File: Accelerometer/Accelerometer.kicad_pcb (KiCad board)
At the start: 2 copper layers, 50 x 31 mm, 8 parts, among them U1 KX134-1211

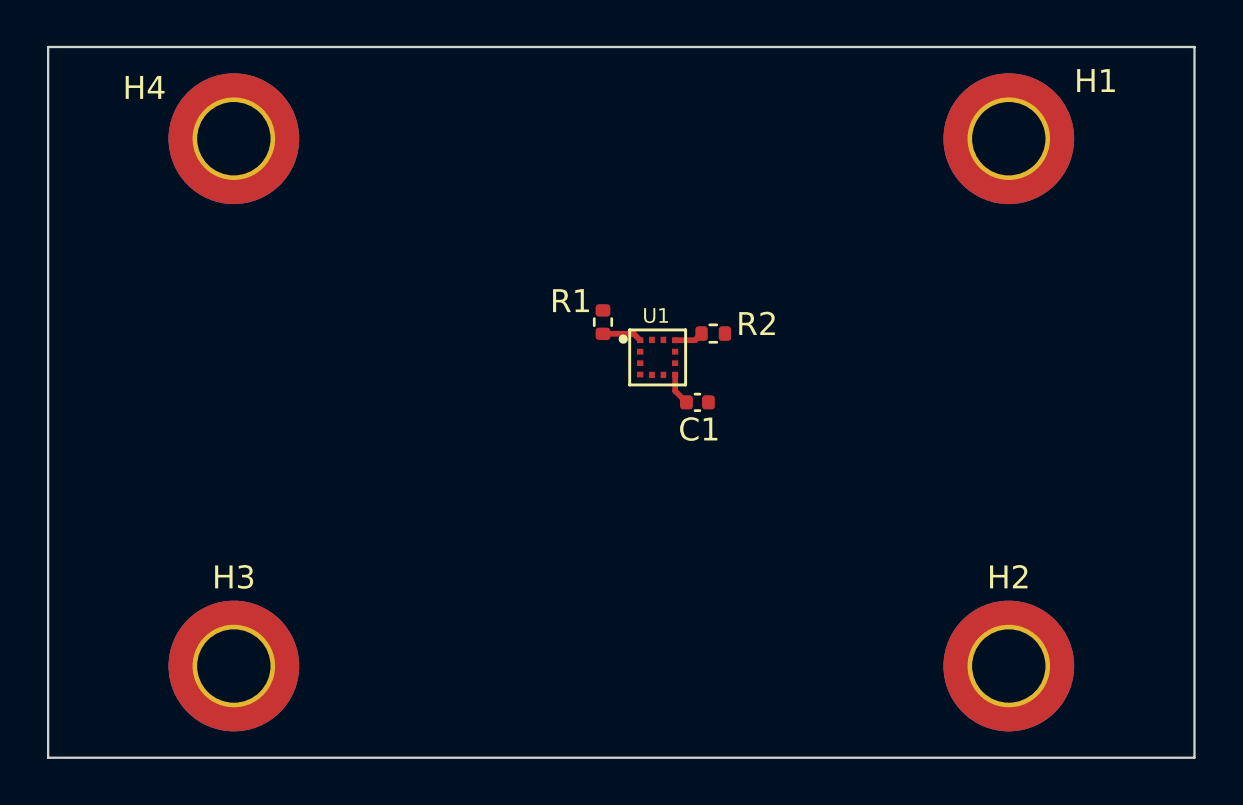
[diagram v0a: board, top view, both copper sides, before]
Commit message: Route sensors, IMU and radio board
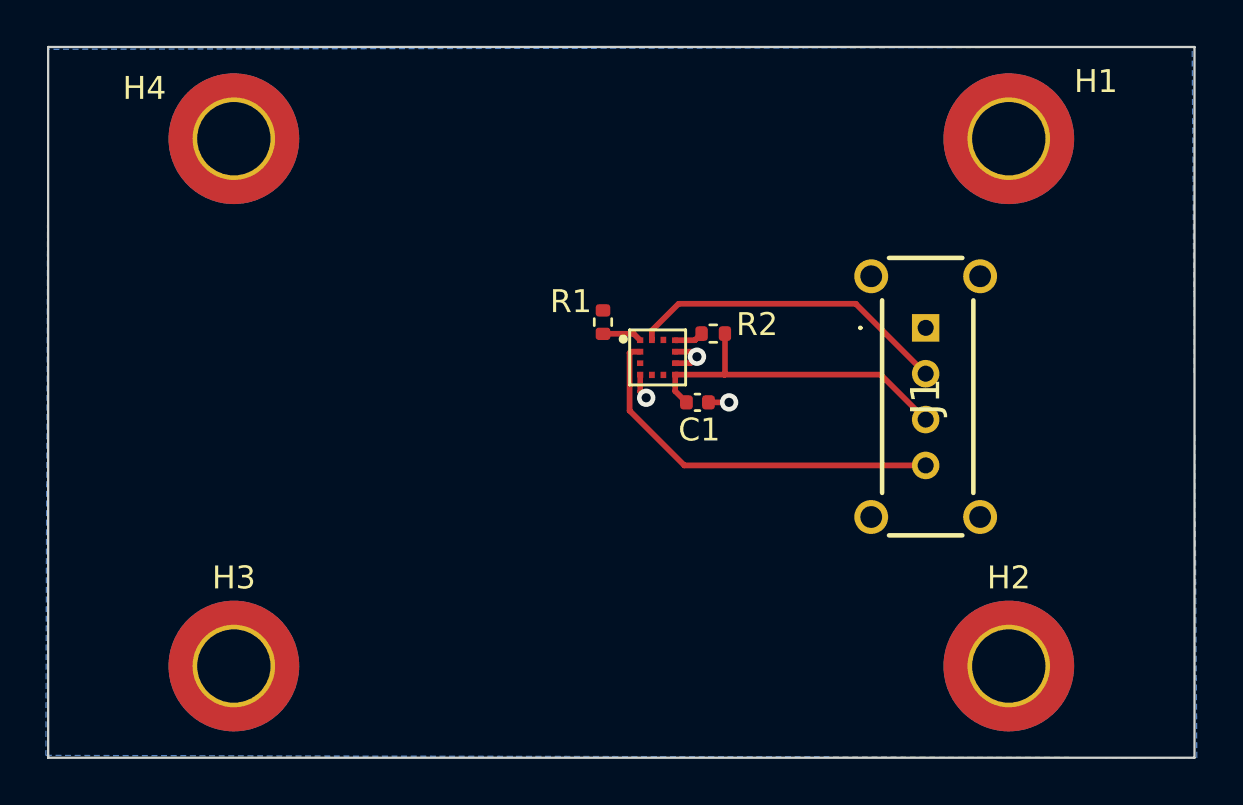
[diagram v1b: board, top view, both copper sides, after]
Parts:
- added J1: M80-8770405, KiCad:M808770405, F.Cu at (151.1, 88.7)
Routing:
- net /SDA: track 0.00 -> 16.9 mm
- net /SCL: track 0.00 -> 14.1 mm
- net +3.3V: track 1.41 -> 15.0 mm
- net GND: track 0.00 -> 4.13 mm, vias 0 -> 3
- added copper zone on B.Cu, net GND
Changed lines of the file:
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@@
   (net 8 "unconnected-(U1-NC-Pad11)")
   (net 9 "/SCL")
+  (net 10 "unconnected-(J1-Pad1)")
+  (net 11 "unconnected-(J1-PadMH1)")
+  (net 12 "unconnected-(J1-PadMH2)")
+  (net 13 "unconnected-(J1-PadMH3)")
+  (net 14 "unconnected-(J1-PadMH4)")
   (footprint "Resistor_SMD:R_0402_1005Metric" (layer "F.Cu")
     (at 141.81 88.9)
@@
       (pinfunction "1") (pintype "input"))
   )
+  (footprint "KiCad:M808770405" (layer "F.Cu")
+    (at 151.075 88.65 90)
+    (descr "M80-8770405-2")
+    (tags "Connector")
+    (property "Arrow Part Number" "")
+    (property "Arrow Price/Stock" "")
+    (property "Height" "5.56")
+    (property "Manufacturer_Name" "Harwin")
+    (property "Manufacturer_Part_Number" "M80-8770405")
+    (property "Mouser Part Number" "855-M80-8770405")
+    (property "Mouser Price/Stock" "https://www.mouser.co.uk/ProductDetail/Harwin/M80-8770405?qs=3tymCvhQ29ZPq83M%252Bf8kIA%3D%3D")
+    (property "Sheetfile" "Accelerometer.kicad_sch")
+    (property "Sheetname" "")
+    (property "ki_description" "Datamate L-Tek SIL Male Vertical 3mm Throughboard Connector, latched, gold, 4 contacts")
+    (attr through_hole)
+    (fp_text reference "J1" (at -3 0 90) (layer "F.SilkS")
+        (effects (font (size 1.27 1.27) (thickness 0.254)))
+    )
+    (fp_text value "M80-8770405" (at -3 0 90) (layer "F.SilkS") hide
+        (effects (font (size 1.27 1.27) (thickness 0.254)))
+    )
+    (fp_text user "${REFERENCE}" (at -3 0 90) (layer "F.Fab")
+        (effects (font (size 1.27 1.27) (thickness 0.254)))
+    )
+    (fp_line (start -9.05 1.6) (end -9.05 -1.6)
+      (stroke (width 0.2) (type solid)) (layer "F.SilkS"))
+    (fp_line (start 0 -2.9) (end 0 -2.9)
+      (stroke (width 0.1) (type solid)) (layer "F.SilkS"))
+    (fp_line (start 0 -2.8) (end 0 -2.8)
+      (stroke (width 0.1) (type solid)) (layer "F.SilkS"))
+    (fp_line (start 1.2 -1.9) (end -7.2 -1.9)
+      (stroke (width 0.2) (type solid)) (layer "F.SilkS"))
+    (fp_line (start 1.2 2.08) (end -7.2 2.08)
+      (stroke (width 0.2) (type solid)) (layer "F.SilkS"))
+    (fp_line (start 3.05 -1.6) (end 3.05 1.6)
+      (stroke (width 0.2) (type solid)) (layer "F.SilkS"))
+    (fp_arc (start 0 -2.9) (mid 0.05 -2.85) (end 0 -2.8)
+      (stroke (width 0.1) (type solid)) (layer "F.SilkS"))
+    (fp_arc (start 0 -2.8) (mid -0.05 -2.85) (end 0 -2.9)
+      (stroke (width 0.1) (type solid)) (layer "F.SilkS"))
+    (fp_line (start -10.05 -4.114) (end -10.05 4.114)
+      (stroke (width 0.1) (type solid)) (layer "F.CrtYd"))
+    (fp_line (start -10.05 4.114) (end 4.05 4.114)
+      (stroke (width 0.1) (type solid)) (layer "F.CrtYd"))
+    (fp_line (start 4.05 -4.114) (end -10.05 -4.114)
+      (stroke (width 0.1) (type solid)) (layer "F.CrtYd"))
+    (fp_line (start 4.05 4.114) (end 4.05 -4.114)
+      (stroke (width 0.1) (type solid)) (layer "F.CrtYd"))
+    (fp_line (start -9.05 -1.9) (end 3.05 -1.9)
+      (stroke (width 0.1) (type solid)) (layer "F.Fab"))
+    (fp_line (start -9.05 2.08) (end -9.05 -1.9)
+      (stroke (width 0.1) (type solid)) (layer "F.Fab"))
+    (fp_line (start 3.05 -1.9) (end 3.05 2.08)
+      (stroke (width 0.1) (type solid)) (layer "F.Fab"))
+    (fp_line (start 3.05 2.08) (end -9.05 2.08)
+      (stroke (width 0.1) (type solid)) (layer "F.Fab"))
+    (pad "1" thru_hole rect (at 0 0 90) (size 1.2 1.2) (drill 0.7) (layers "*.Cu" "*.Mask")
+      (net 10 "unconnected-(J1-Pad1)") (pinfunction "1") (pintype "passive+no_connect"))
+    (pad "2" thru_hole circle (at -2 0 90) (size 1.2 1.2) (drill 0.7) (layers "*.Cu" "*.Mask")
+      (net 9 "/SCL") (pinfunction "2") (pintype "passive"))
+    (pad "3" thru_hole circle (at -4 0 90) (size 1.2 1.2) (drill 0.7) (layers "*.Cu" "*.Mask")
+      (net 1 "+3.3V") (pinfunction "3") (pintype "passive"))
+    (pad "4" thru_hole circle (at -6 0 90) (size 1.2 1.2) (drill 0.7) (layers "*.Cu" "*.Mask")
+      (net 5 "/SDA") (pinfunction "4") (pintype "passive"))
+    (pad "MH1" thru_hole circle (at 2.25 -2.375 90) (size 1.478 1.478) (drill 0.95) (layers "*.Cu" "*.Mask")
+      (net 11 "unconnected-(J1-PadMH1)") (pinfunction "MH1") (pintype "passive+no_connect"))
+    (pad "MH2" thru_hole circle (at 2.25 2.375 90) (size 1.478 1.478) (drill 0.95) (layers "*.Cu" "*.Mask")
+      (net 12 "unconnected-(J1-PadMH2)") (pinfunction "MH2") (pintype "passive+no_connect"))
+    (pad "MH3" thru_hole circle (at -8.25 2.375 90) (size 1.478 1.478) (drill 0.95) (layers "*.Cu" "*.Mask")
+      (net 13 "unconnected-(J1-PadMH3)") (pinfunction "MH3") (pintype "passive+no_connect"))
+    (pad "MH4" thru_hole circle (at -8.25 -2.375 90) (size 1.478 1.478) (drill 0.95) (layers "*.Cu" "*.Mask")
+      (net 14 "unconnected-(J1-PadMH4)") (pinfunction "MH4") (pintype "passive+no_connect"))
+    (model "M80-8770405.stp"
+      (offset (xyz 0 0 0))
+      (scale (xyz 1 1 1))
+      (rotate (xyz 0 0 0))
+    )
+  )
   (footprint "XDCR_KX003-1077:XDCR_KX003-1077" (layer "F.Cu")
     (at 139.385 89.94)
@@
     (property "ki_keywords" "KX134-1211")
     (attr smd)
-    (fp_text reference "U1" (at -0.068 -1.8064) (layer "F.SilkS")
+    (fp_text reference "U1" (at -0.068 -1.8064) (layer "F.SilkS") hide
         (effects (font (size 0.64 0.64) (thickness 0.15)))
     )
@@
     (stroke (width 0.1) (type default)) (layer "Edge.Cuts"))
   (segment (start 140.1475 90.69) (end 140.1475 91.4075) (width 0.25) (layer "F.Cu") (net 1))
+  (segment (start 142.32 90.67) (end 142.3 90.69) (width 0.25) (layer "F.Cu") (net 1))
+  (segment (start 149.115 90.69) (end 151.075 92.65) (width 0.25) (layer "F.Cu") (net 1))
+  (segment (start 142.32 88.9) (end 142.32 90.67) (width 0.25) (layer "F.Cu") (net 1))
+  (segment (start 140.1475 90.69) (end 142.3 90.69) (width 0.25) (layer "F.Cu") (net 1))
+  (segment (start 142.3 90.69) (end 149.115 90.69) (width 0.25) (layer "F.Cu") (net 1))
   (segment (start 140.1475 91.4075) (end 140.64 91.9) (width 0.25) (layer "F.Cu") (net 1))
+  (segment (start 140.1475 90.19) (end 140.818393 90.19) (width 0.25) (layer "F.Cu") (net 2))
+  (segment (start 140.818393 90.19) (end 141.099434 89.908959) (width 0.25) (layer "F.Cu") (net 2))
+  (segment (start 138.6225 90.69) (end 138.6225 91.438) (width 0.25) (layer "F.Cu") (net 2))
+  (segment (start 138.6225 91.438) (end 138.8845 91.7) (width 0.25) (layer "F.Cu") (net 2))
+  (segment (start 140.880475 89.69) (end 141.099434 89.908959) (width 0.25) (layer "F.Cu") (net 2))
+  (segment (start 141.6 91.9) (end 142.5 91.9) (width 0.25) (layer "F.Cu") (net 2))
+  (segment (start 140.1475 89.69) (end 140.880475 89.69) (width 0.25) (layer "F.Cu") (net 2))
+  (via (at 138.8845 91.7) (size 0.8) (drill 0.4) (layers "F.Cu" "B.Cu") (net 2))
+  (via (at 141.099434 89.908959) (size 0.8) (drill 0.4) (layers "F.Cu" "B.Cu") (net 2))
+  (via (at 142.5 91.9) (size 0.8) (drill 0.4) (layers "F.Cu" "B.Cu") (net 2))
   (segment (start 137 88.91) (end 138.3425 88.91) (width 0.25) (layer "F.Cu") (net 3))
   (segment (start 138.3425 88.91) (end 138.6225 89.19) (width 0.25) (layer "F.Cu") (net 3))
   (segment (start 140.1475 89.19) (end 141.01 89.19) (width 0.25) (layer "F.Cu") (net 4))
   (segment (start 141.01 89.19) (end 141.3 88.9) (width 0.25) (layer "F.Cu") (net 4))
+  (segment (start 138.16 89.74) (end 138.16 92.26) (width 0.25) (layer "F.Cu") (net 5))
+  (segment (start 138.21 89.69) (end 138.16 89.74) (width 0.25) (layer "F.Cu") (net 5))
+  (segment (start 140.55 94.65) (end 151.075 94.65) (width 0.25) (layer "F.Cu") (net 5))
+  (segment (start 138.16 92.26) (end 140.55 94.65) (width 0.25) (layer "F.Cu") (net 5))
+  (segment (start 138.6225 89.69) (end 138.21 89.69) (width 0.25) (layer "F.Cu") (net 5))
+  (segment (start 139.135 89.1775) (end 139.135 88.765) (width 0.25) (layer "F.Cu") (net 9))
+  (segment (start 139.135 88.765) (end 140.3 87.6) (width 0.25) (layer "F.Cu") (net 9))
+  (segment (start 148.025 87.6) (end 151.075 90.65) (width 0.25) (layer "F.Cu") (net 9))
+  (segment (start 140.3 87.6) (end 148.025 87.6) (width 0.25) (layer "F.Cu") (net 9))
+  (zone (net 2) (net_name "GND") (layer "B.Cu") (hatch edge 0.5)
+    (connect_pads (clearance 0.3))
+    (min_thickness 0.25) (filled_areas_thickness no)
+    (fill yes (thermal_gap 0.5) (thermal_bridge_width 0.5))
+    (polygon
+      (pts
+        (xy 112.8 76.5)
+        (xy 112.7 107.3)
+        (xy 162.9 107.4)
+        (xy 162.7 76.4)
+      )
+    )
+  )
 )

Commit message: Done with most of the boards
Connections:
- J1 pad 1: unconnected-(J1-Pad1) -> GND
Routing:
- net GND: track 4.13 -> 30.6 mm
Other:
- board text added: "SCL"
- board text added: "SDA"
- board text added: "Vin"
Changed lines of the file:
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@@
   (net 8 "unconnected-(U1-NC-Pad11)")
   (net 9 "/SCL")
-  (net 10 "unconnected-(J1-Pad1)")
-  (net 11 "unconnected-(J1-PadMH1)")
-  (net 12 "unconnected-(J1-PadMH2)")
-  (net 13 "unconnected-(J1-PadMH3)")
-  (net 14 "unconnected-(J1-PadMH4)")
+  (net 10 "unconnected-(J1-PadMH1)")
+  (net 11 "unconnected-(J1-PadMH2)")
+  (net 12 "unconnected-(J1-PadMH3)")
+  (net 13 "unconnected-(J1-PadMH4)")
   (footprint "Resistor_SMD:R_0402_1005Metric" (layer "F.Cu")
     (at 141.81 88.9)
@@
       (stroke (width 0.1) (type solid)) (layer "F.Fab"))
     (pad "1" thru_hole rect (at 0 0 90) (size 1.2 1.2) (drill 0.7) (layers "*.Cu" "*.Mask")
-      (net 10 "unconnected-(J1-Pad1)") (pinfunction "1") (pintype "passive+no_connect"))
+      (net 2 "GND") (pinfunction "1") (pintype "passive"))
     (pad "2" thru_hole circle (at -2 0 90) (size 1.2 1.2) (drill 0.7) (layers "*.Cu" "*.Mask")
       (net 9 "/SCL") (pinfunction "2") (pintype "passive"))
@@
       (net 5 "/SDA") (pinfunction "4") (pintype "passive"))
     (pad "MH1" thru_hole circle (at 2.25 -2.375 90) (size 1.478 1.478) (drill 0.95) (layers "*.Cu" "*.Mask")
-      (net 11 "unconnected-(J1-PadMH1)") (pinfunction "MH1") (pintype "passive+no_connect"))
+      (net 10 "unconnected-(J1-PadMH1)") (pinfunction "MH1") (pintype "passive+no_connect"))
     (pad "MH2" thru_hole circle (at 2.25 2.375 90) (size 1.478 1.478) (drill 0.95) (layers "*.Cu" "*.Mask")
-      (net 12 "unconnected-(J1-PadMH2)") (pinfunction "MH2") (pintype "passive+no_connect"))
+      (net 11 "unconnected-(J1-PadMH2)") (pinfunction "MH2") (pintype "passive+no_connect"))
     (pad "MH3" thru_hole circle (at -8.25 2.375 90) (size 1.478 1.478) (drill 0.95) (layers "*.Cu" "*.Mask")
-      (net 13 "unconnected-(J1-PadMH3)") (pinfunction "MH3") (pintype "passive+no_connect"))
+      (net 12 "unconnected-(J1-PadMH3)") (pinfunction "MH3") (pintype "passive+no_connect"))
     (pad "MH4" thru_hole circle (at -8.25 -2.375 90) (size 1.478 1.478) (drill 0.95) (layers "*.Cu" "*.Mask")
-      (net 14 "unconnected-(J1-PadMH4)") (pinfunction "MH4") (pintype "passive+no_connect"))
+      (net 13 "unconnected-(J1-PadMH4)") (pinfunction "MH4") (pintype "passive+no_connect"))
     (model "M80-8770405.stp"
       (offset (xyz 0 0 0))
@@
   (gr_line (start 162.8 107.4) (end 162.8 76.4)
     (stroke (width 0.1) (type default)) (layer "Edge.Cuts"))
+  (gr_text "SDA" (at 144.6 95.5) (layer "F.SilkS")
+    (effects (font (size 1 1) (thickness 0.15)))
+  )
+  (gr_text "SCL" (at 145.6 86.9) (layer "F.SilkS")
+    (effects (font (size 0.9 0.8) (thickness 0.15)))
+  )
+  (gr_text "Vin" (at 145.2 89.9) (layer "F.SilkS")
+    (effects (font (size 1 1) (thickness 0.15)))
+  )
   (segment (start 140.1475 90.69) (end 140.1475 91.4075) (width 0.25) (layer "F.Cu") (net 1))
   (segment (start 142.32 90.67) (end 142.3 90.69) (width 0.25) (layer "F.Cu") (net 1))
@@
   (via (at 141.099434 89.908959) (size 0.8) (drill 0.4) (layers "F.Cu" "B.Cu") (net 2))
   (via (at 142.5 91.9) (size 0.8) (drill 0.4) (layers "F.Cu" "B.Cu") (net 2))
+  (segment (start 146.3 88.75) (end 146.4 88.65) (width 0.25) (layer "B.Cu") (net 2))
+  (segment (start 138.9 91.7) (end 141.3 94.1) (width 0.25) (layer "B.Cu") (net 2))
+  (segment (start 144.95 88.65) (end 146.4 88.65) (width 0.25) (layer "B.Cu") (net 2))
+  (segment (start 146.3 91.6) (end 146.3 88.75) (width 0.25) (layer "B.Cu") (net 2))
+  (segment (start 144.5 91.9) (end 146 91.9) (width 0.25) (layer "B.Cu") (net 2))
+  (segment (start 141.3 94.1) (end 144.4 94.1) (width 0.25) (layer "B.Cu") (net 2))
+  (segment (start 141.099434 89.908959) (end 143.691041 89.908959) (width 0.25) (layer "B.Cu") (net 2))
+  (segment (start 143.691041 89.908959) (end 144.95 88.65) (width 0.25) (layer "B.Cu") (net 2))
+  (segment (start 144.4 92) (end 144.5 91.9) (width 0.25) (layer "B.Cu") (net 2))
+  (segment (start 146 91.9) (end 146.3 91.6) (width 0.25) (layer "B.Cu") (net 2))
+  (segment (start 142.5 91.9) (end 144.5 91.9) (width 0.25) (layer "B.Cu") (net 2))
+  (segment (start 144.4 94.1) (end 144.4 92) (width 0.25) (layer "B.Cu") (net 2))
+  (segment (start 146.4 88.65) (end 151.075 88.65) (width 0.25) (layer "B.Cu") (net 2))
+  (segment (start 138.8845 91.7) (end 138.9 91.7) (width 0.25) (layer "B.Cu") (net 2))
+  (segment (start 138.8845 91.7) (end 139.2 91.7) (width 0.25) (layer "B.Cu") (net 2))
   (segment (start 137 88.91) (end 138.3425 88.91) (width 0.25) (layer "F.Cu") (net 3))
   (segment (start 138.3425 88.91) (end 138.6225 89.19) (width 0.25) (layer "F.Cu") (net 3))

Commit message: Started fixing layouts
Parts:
- removed H1, H2, H3, H4: MountingHole_Pad, MountingHole:MountingHole_3.2mm_M3_ISO7380_Pad_TopBottom
- removed R1, R2: 4.7k, Resistor_SMD:R_0402_1005Metric
- added JP1: SolderJumper_3_Open, Jumper:SolderJumper-3_P1.3mm_Open_RoundedPad1.0x1.5mm_NumberLabels, F.Cu at (131.5, 89.5)
- added R3: 1.5k, Resistor_SMD:R_0201_0603Metric_Pad0.64x0.40mm_HandSolder, F.Cu at (144.0, 87.2)
- added R4: 1.5k, Resistor_SMD:R_0201_0603Metric_Pad0.64x0.40mm_HandSolder, F.Cu at (142.2, 92.5)
- moved C1 7.33 mm to (143.6, 85.0), turned to 180 degrees
- moved U1 2.70 mm to (136.7, 90.3)
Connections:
- J1 pad 1: GND -> +3.3V
- J1 pad 3: +3.3V -> /SDA
- J1 pad 4: /SDA -> GND
- U1 pad 10: Net-(U1-nCS) -> +3.3V
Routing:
- net +3.3V: track 15.0 -> 35.1 mm, vias 0 -> 2
- net GND: track 30.6 -> 15.8 mm, vias 3 -> 5
- net /SCL: track 14.1 -> 20.1 mm
- net /SDA: track 16.9 -> 22.2 mm
- net Net-(JP1-C): track 1.74 -> 4.43 mm
- net Net-(U1-nCS): track 1.27 -> 0.00 mm
- added copper zone on B.Cu, net +3.3V
- added copper zone on F.Cu, net GND
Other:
- board text added: "GND"
- board text added: "VDD"

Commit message: LC24 PCBs
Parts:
- removed J1: M80-8770405, KiCad:M808770405
- added C2: 100nF, Capacitor_SMD:C_0402_1005Metric, F.Cu at (157.9, 73.3)
- added C3: 100nF, Capacitor_SMD:C_0402_1005Metric, F.Cu at (157.9, 77.7)
- added C4: 100n, Capacitor_SMD:C_0402_1005Metric, F.Cu at (118.0, 51.6)
- added C5: 100n, Capacitor_SMD:C_0402_1005Metric, F.Cu at (118.0, 56.1)
- added H1: MountingHole_Pad, Mounting_Wuerth:Mounting_Wuerth_WA-SMSI-M1.6_H1mm_9774010633, F.Cu at (137.2, 45.7)
- added H2: MountingHole_Pad, Mounting_Wuerth:Mounting_Wuerth_WA-SMSI-M1.6_H1mm_9774010633, F.Cu at (138.9, 133.0)
- added H3: MountingHole_Pad, Mounting_Wuerth:Mounting_Wuerth_WA-SMSI-M1.6_H1mm_9774010633, F.Cu at (88.5, 78.0)
- added H4: MountingHole_Pad, Mounting_Wuerth:Mounting_Wuerth_WA-SMSI-M1.6_H1mm_9774010633, F.Cu at (178.3, 97.4)
- added IC1: FRAM, Package_SO:SOIC-8-1EP_3.9x4.9mm_P1.27mm_EP2.29x3mm, F.Cu at (107.6, 110.7)
- added IC2: BMI088, BMI088:QFN_BMI085_BOS, F.Cu at (97.3, 92.6)
- added J2: M80-8770422, Harwin-M80-8770422:CONN_M80-87704_HRW, F.Cu at (150.9, 87.6)
- added JP11: SolderJumper_2_Open, Jumper:SolderJumper-2_P1.3mm_Open_RoundedPad1.0x1.5mm, F.Cu at (104.9, 104.0)
- added JP2: SolderJumper_3_Open, Jumper:SolderJumper-3_P1.3mm_Open_RoundedPad1.0x1.5mm_NumberLabels, F.Cu at (150.2, 65.9)
- added JP3: SolderJumper_2_Open, Jumper:SolderJumper-2_P1.3mm_Open_RoundedPad1.0x1.5mm, F.Cu at (96.0, 111.2)
- added JP4: SolderJumper_2_Open, Jumper:SolderJumper-2_P1.3mm_Open_RoundedPad1.0x1.5mm, F.Cu at (96.0, 106.6)
- added JP5: SolderJumper_2_Open, Jumper:SolderJumper-2_P1.3mm_Open_RoundedPad1.0x1.5mm, F.Cu at (96.0, 116.0)
- added JP6: SolderJumper_3_Open, Jumper:SolderJumper-3_P1.3mm_Open_RoundedPad1.0x1.5mm_NumberLabels, F.Cu at (89.3, 93.2)
- added JP7: SolderJumper_3_Open, Jumper:SolderJumper-3_P1.3mm_Open_RoundedPad1.0x1.5mm_NumberLabels, F.Cu at (106.1, 94.5)
- added U2: BMP280, Package_LGA:Bosch_LGA-8_2x2.5mm_P0.65mm_ClockwisePinNumbering, F.Cu at (151.1, 73.5)
- U1: footprint XDCR_KX003-1077:XDCR_KX003-1077 -> KX134:LGA12_2X2X0P9_ROM
- moved C1 35.6 mm to (117.9, 60.3), turned to 0 degrees
- moved U1 32.1 mm to (116.6, 65.3)
- moved JP1 32.1 mm to (110.8, 65.0)
- moved R4 18.6 mm to (160.8, 93.2), turned to 180 degrees
- moved R3 17.1 mm to (161.0, 89.3)
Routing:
- net +3.3V: track 35.1 -> 250.3 mm, vias 2 -> 4
- net /SCL: track 20.1 -> 141.5 mm, vias 0 -> 7
- net /SDA: track 22.2 -> 140.7 mm, vias 0 -> 2
- net GND: track 15.8 -> 37.7 mm, vias 5 -> 11
- net Net-(IC1-A2): track 0.00 -> 10.5 mm
- net Net-(IC1-A0): track 0.00 -> 9.44 mm
- net Net-(IC1-A1): track 0.00 -> 8.90 mm
- net Net-(IC2-SDO2): track 0.00 -> 8.42 mm
- net Net-(IC1-VDD): track 0.00 -> 7.37 mm
- net Net-(JP2-C): track 0.00 -> 6.84 mm
- net Net-(IC2-SDO1): track 0.00 -> 6.72 mm
- net Net-(JP1-C): track 4.43 -> 5.21 mm
- removed copper zone on B.Cu, net +3.3V
- removed copper zone on B.Cu, net GND
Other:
- board size 50 x 31 mm -> 101.1 x 101.1 mm
- board text added: "Rocket Avionics"
- board text added: "USST"
- board text removed: "Vin"
